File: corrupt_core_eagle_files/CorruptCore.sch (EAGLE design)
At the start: 89 parts, among them IC1 MEGA8-P, K1 DTS-3, K10 DTS-3, K11 DTS-3, K12 DTS-3, K13 DTS-3, K14 DTS-3, K15 DTS-3, K16 DTS-3, K2 DTS-3, K3 DTS-3, K4 DTS-3, K5 DTS-3, K6 DTS-3, K7 DTS-3, K8 DTS-3, K9 DTS-3, Q1 TRANS_NPN-MMBTA42, Q2 TRANS_NPN-MMBTA42, Q3 TRANS_NPN-MMBTA42, Q4 TRANS_NPN-MMBTA42, Y1 16MHz

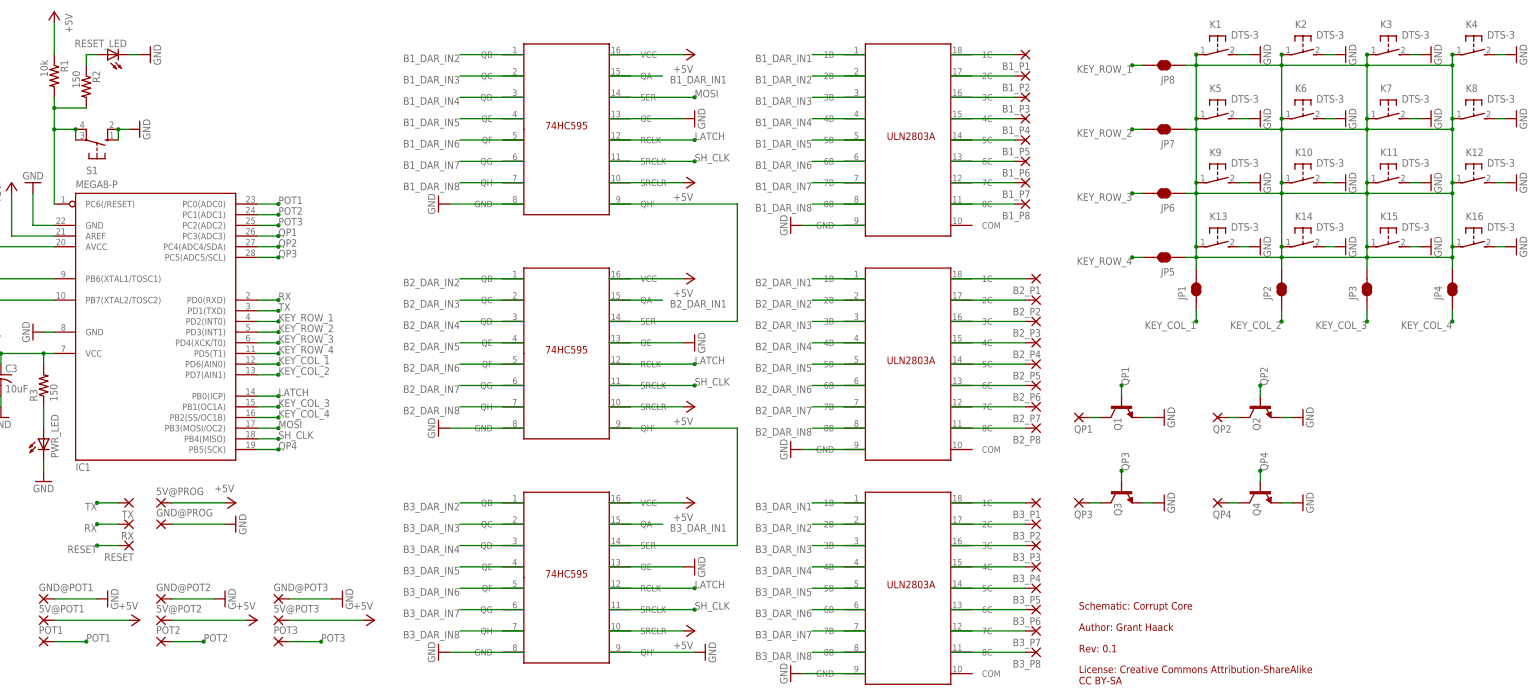
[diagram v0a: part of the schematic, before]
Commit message: -started laying out board -further organized schematic
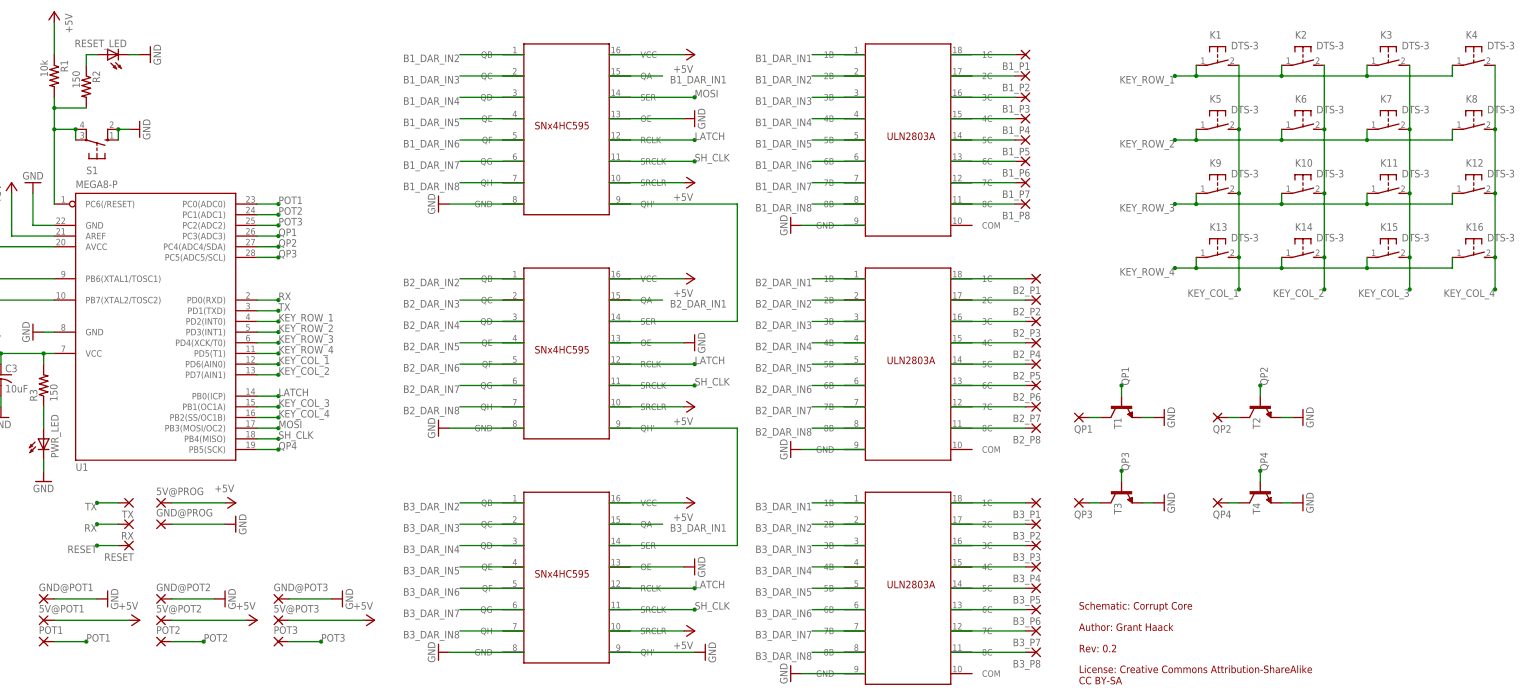
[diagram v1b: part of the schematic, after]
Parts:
- removed JP1, JP2, JP3, JP4, JP5, JP6, JP7, JP8: JUMPER-SMT_2_NC_TRACE_NO-SILK, SparkFun-Jumpers:JUMPER-SMT_2_NC_TRACE_NO-SILK
- removed U$1, U$3, U$5: SN74HC595N, CorruptCore:SN74HC595N
- removed U$2, U$4, U$6: ULN2803A, CorruptCore:ULN2803A
- added U2, U3, U4: SNX4HC595SOIC16, CorruptCore:SNX4HC595SOIC16
- added U5, U6, U7: ULN2803ASOIC18, CorruptCore:ULN2803ASOIC18
- 5V@POT1, 5V@POT2, 5V@POT3, 5V@PROG, B1_P1, B1_P2, B1_P3, B1_P4, B1_P5, B1_P6, B1_P7, B1_P8, B2_P1, B2_P2, B2_P3, B2_P4, B2_P5, B2_P6, B2_P7, B2_P8, B3_P1, B3_P2, B3_P3, B3_P4, B3_P5, B3_P6, B3_P7, B3_P8, GND@POT1, GND@POT2, GND@POT3, GND@PROG, POT1, POT2, POT3, QP1, QP2, QP3, QP4, RESET, RX, TX: device wirepad:2,54/1,1 -> wirepad:1,6/0,8
- renumbered IC1 to U1, Q1 to T1, Q2 to T2, Q3 to T3, Q4 to T4
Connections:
- removed net N$5: JP1.2, JP2.2, JP3.2, JP4.2, JP5.1, JP6.1, JP7.1, JP8.1, K1.1, K10.1, K11.1, K12.1, K13.1, K14.1, K15.1, K16.1, K2.1, K3.1, K4.1, K5.1, K6.1, K7.1, K8.1, K9.1
- net +5V: now also U2.SRCLR, U2.VCC, U3.SRCLR, U3.VCC, U4.SRCLR, U4.VCC; no longer U$1.SRCLR, U$1.VCC, U$3.SRCLR, U$3.VCC, U$5.SRCLR, U$5.VCC
- net B1_DAR_IN1: now also U2.QA, U5.1B; no longer U$1.QA, U$2.1B
- net B1_DAR_IN2: now also U2.QB, U5.2B; no longer U$1.QB, U$2.2B
- net B1_DAR_IN3: now also U2.QC, U5.3B; no longer U$1.QC, U$2.3B
- net B1_DAR_IN4: now also U2.QD, U5.4B; no longer U$1.QD, U$2.4B
- net B1_DAR_IN5: now also U2.QE, U5.5B; no longer U$1.QE, U$2.5B
- net B1_DAR_IN6: now also U2.QF, U5.6B; no longer U$1.QF, U$2.6B
- net B1_DAR_IN7: now also U2.QG, U5.7B; no longer U$1.QG, U$2.7B
- net B1_DAR_IN8: now also U2.QH, U5.8B; no longer U$1.QH, U$2.8B
- net B1_P1: now also U5.1C; no longer U$2.1C
- net B1_P2: now also U5.2C; no longer U$2.2C
- net B1_P3: now also U5.3C; no longer U$2.3C
- net B1_P4: now also U5.4C; no longer U$2.4C
- net B1_P5: now also U5.5C; no longer U$2.5C
- net B1_P6: now also U5.6C; no longer U$2.6C
- net B1_P7: now also U5.7C; no longer U$2.7C
- net B1_P8: now also U5.8C; no longer U$2.8C
- net B2_DAR_IN1: now also U3.QA, U6.1B; no longer U$3.QA, U$4.1B
- net B2_DAR_IN2: now also U3.QB, U6.2B; no longer U$3.QB, U$4.2B
- net B2_DAR_IN3: now also U3.QC, U6.3B; no longer U$3.QC, U$4.3B
- net B2_DAR_IN4: now also U3.QD, U6.4B; no longer U$3.QD, U$4.4B
- net B2_DAR_IN5: now also U3.QE, U6.5B; no longer U$3.QE, U$4.5B
- net B2_DAR_IN6: now also U3.QF, U6.6B; no longer U$3.QF, U$4.6B
- net B2_DAR_IN7: now also U3.QG, U6.7B; no longer U$3.QG, U$4.7B
- net B2_DAR_IN8: now also U3.QH, U6.8B; no longer U$3.QH, U$4.8B
- net B2_P1: now also U6.1C; no longer U$4.1C
- net B2_P2: now also U6.2C; no longer U$4.2C
- net B2_P3: now also U6.3C; no longer U$4.3C
- net B2_P4: now also U6.4C; no longer U$4.4C
- net B2_P5: now also U6.5C; no longer U$4.5C
- net B2_P6: now also U6.6C; no longer U$4.6C
- net B2_P7: now also U6.7C; no longer U$4.7C
- net B2_P8: now also U6.8C; no longer U$4.8C
- net B3_DAR_IN1: now also U4.QA, U7.1B; no longer U$5.QA, U$6.1B
- net B3_DAR_IN2: now also U4.QB, U7.2B; no longer U$5.QB, U$6.2B
- net B3_DAR_IN3: now also U4.QC, U7.3B; no longer U$5.QC, U$6.3B
- net B3_DAR_IN4: now also U4.QD, U7.4B; no longer U$5.QD, U$6.4B
- net B3_DAR_IN5: now also U4.QE, U7.5B; no longer U$5.QE, U$6.5B
- net B3_DAR_IN6: now also U4.QF, U7.6B; no longer U$5.QF, U$6.6B
- net B3_DAR_IN7: now also U4.QG, U7.7B; no longer U$5.QG, U$6.7B
- net B3_DAR_IN8: now also U4.QH, U7.8B; no longer U$5.QH, U$6.8B
- net B3_P1: now also U7.1C; no longer U$6.1C
- net B3_P2: now also U7.2C; no longer U$6.2C
- net B3_P3: now also U7.3C; no longer U$6.3C
- net B3_P4: now also U7.4C; no longer U$6.4C
- net B3_P5: now also U7.5C; no longer U$6.5C
- net B3_P6: now also U7.6C; no longer U$6.6C
- net B3_P7: now also U7.7C; no longer U$6.7C
- net B3_P8: now also U7.8C; no longer U$6.8C
- net GND: now also U2.GND, U2.OE, U3.GND, U3.OE, U4.GND, U4.OE, U4.QH', U5.GND, U6.GND, U7.GND; no longer K1.2, K10.2, K11.2, K12.2, K13.2, K14.2, K15.2, K16.2, K2.2, K3.2, K4.2, K5.2, K6.2, K7.2, K8.2, K9.2, U$1.GND, U$1.OE, U$2.GND, U$3.GND, U$3.OE, U$4.GND, U$5.GND, U$5.OE, U$5.QH', U$6.GND
- net KEY_COL_1: now also K1.2, K13.2, K5.2, K9.2; no longer JP1.1
- net KEY_COL_2: now also K10.2, K14.2, K2.2, K6.2; no longer JP2.1
- net KEY_COL_3: now also K11.2, K15.2, K3.2, K7.2; no longer JP3.1
- net KEY_COL_4: now also K12.2, K16.2, K4.2, K8.2; no longer JP4.1
- net KEY_ROW_1: now also K1.1, K2.1, K3.1, K4.1; no longer JP8.2
- net KEY_ROW_2: now also K5.1, K6.1, K7.1, K8.1; no longer JP7.2
- net KEY_ROW_3: now also K10.1, K11.1, K12.1, K9.1; no longer JP6.2
- net KEY_ROW_4: now also K13.1, K14.1, K15.1, K16.1; no longer JP5.2
- net LATCH: now also U2.RCLK, U3.RCLK, U4.RCLK; no longer U$1.RCLK, U$3.RCLK, U$5.RCLK
- net MOSI: now also U2.SER; no longer U$1.SER
- net N$1: now also U2.QH', U3.SER; no longer U$1.QH', U$3.SER
- net N$2: now also U3.QH', U4.SER; no longer U$3.QH', U$5.SER
- net SH_CLK: now also U2.SRCLK, U3.SRCLK, U4.SRCLK; no longer U$1.SRCLK, U$3.SRCLK, U$5.SRCLK
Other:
- note added: "Rev: 0.2"
- note removed: "Rev: 0.1"
- moved on the sheet: K1, K10, K11, K12, K13, K14, K15, K16, K2, K3, K4, K5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

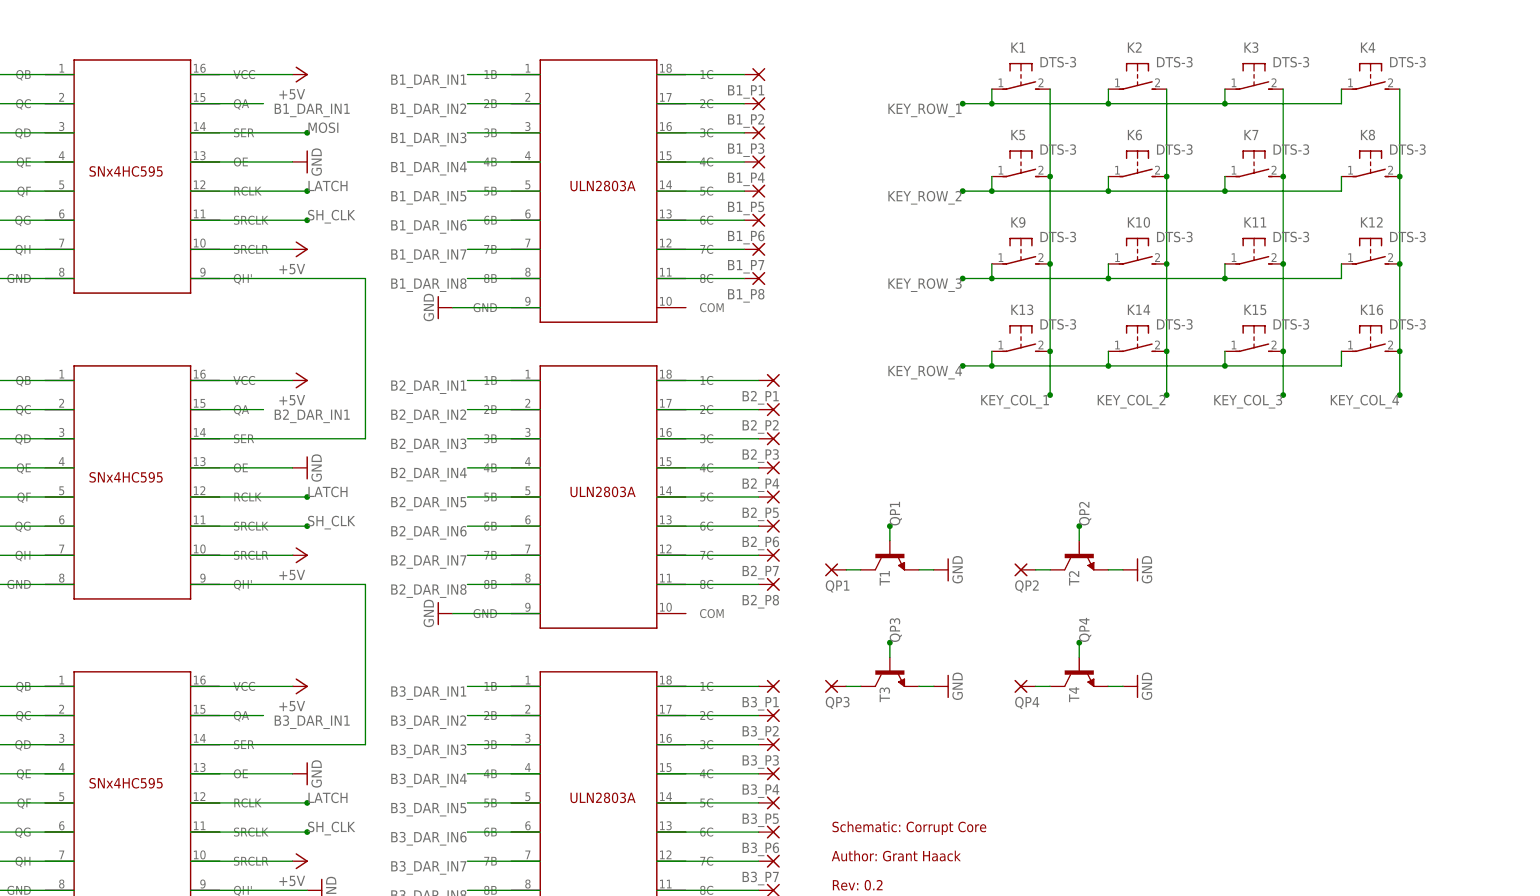
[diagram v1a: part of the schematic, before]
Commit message: -added LTC1799 device to library -added LTC1799 to the schematic -added LTC1799 to the board -small board/schematic cleanup
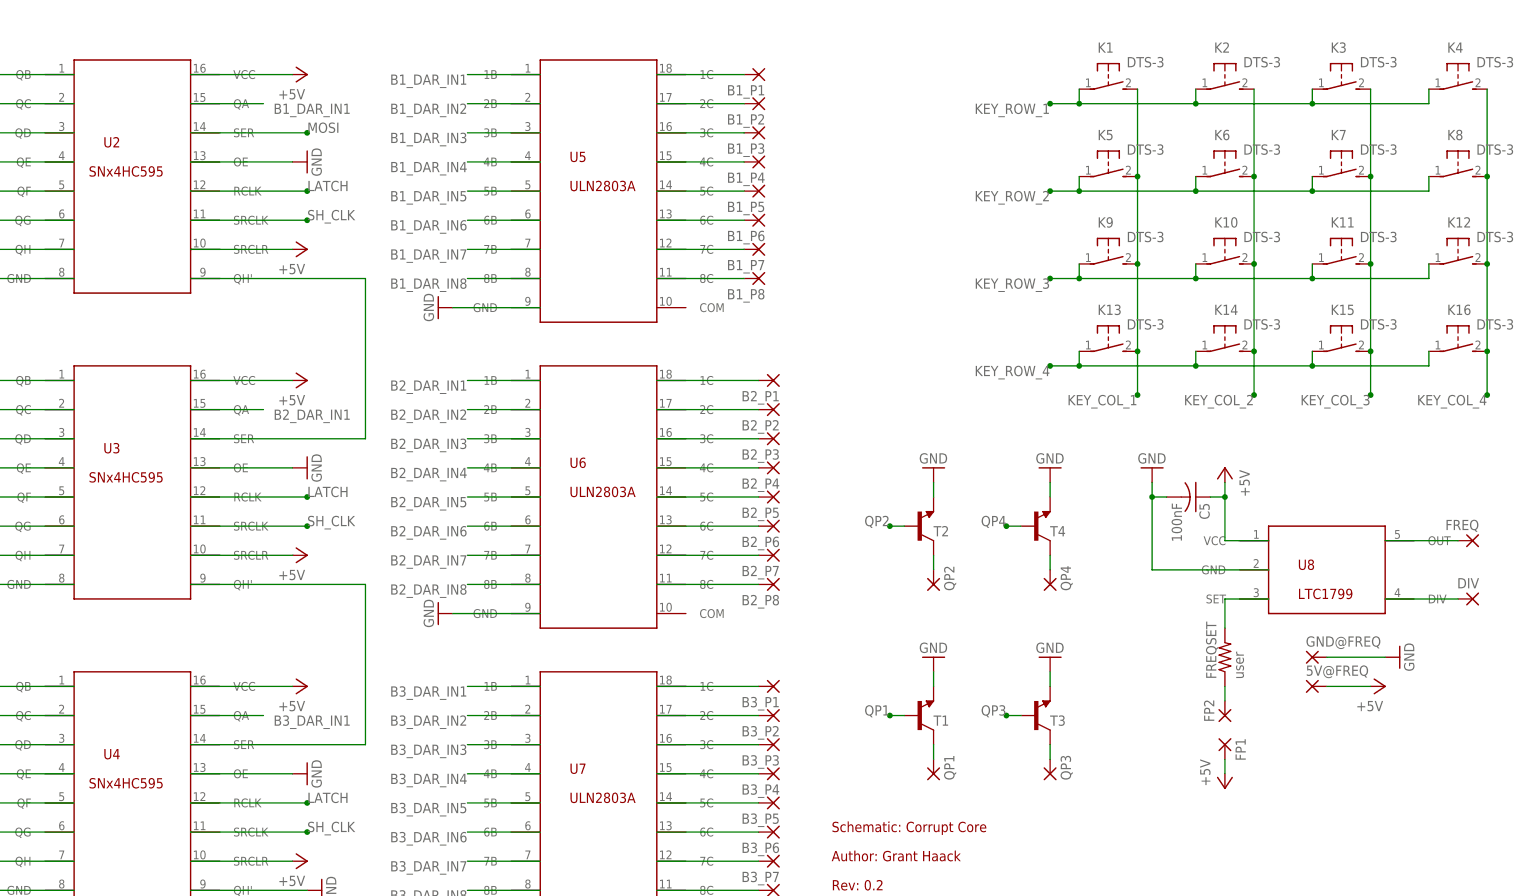
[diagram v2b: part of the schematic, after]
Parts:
- added 5V@FREQ, DIV, FP1, FP2, FREQ, GND@FREQ: (no value), wirepad:1,6/0,8
- added C5: 100nF, resistor:C-USC0805
- added FREQSET: user, resistor:R-US_0207/7
- added U8: LTC1799, CorruptCore:LTC1799
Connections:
- new net N$13: DIV.P, U8.DIV
- new net N$14: FP2.P, FREQSET.1
- new net N$16: FREQSET.2, U8.SET
- new net N$5: FREQ.P, U8.OUT
- net +5V: now also 5V@FREQ.P, C5.1, FP1.P, U8.VCC
- net GND: now also C5.2, GND@FREQ.P, U8.GND
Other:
- moved on the sheet: K1, K10, K11, K12, K13, K14, K15, K16, K2, K3, K4, K5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
